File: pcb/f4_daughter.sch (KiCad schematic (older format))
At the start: 0 parts

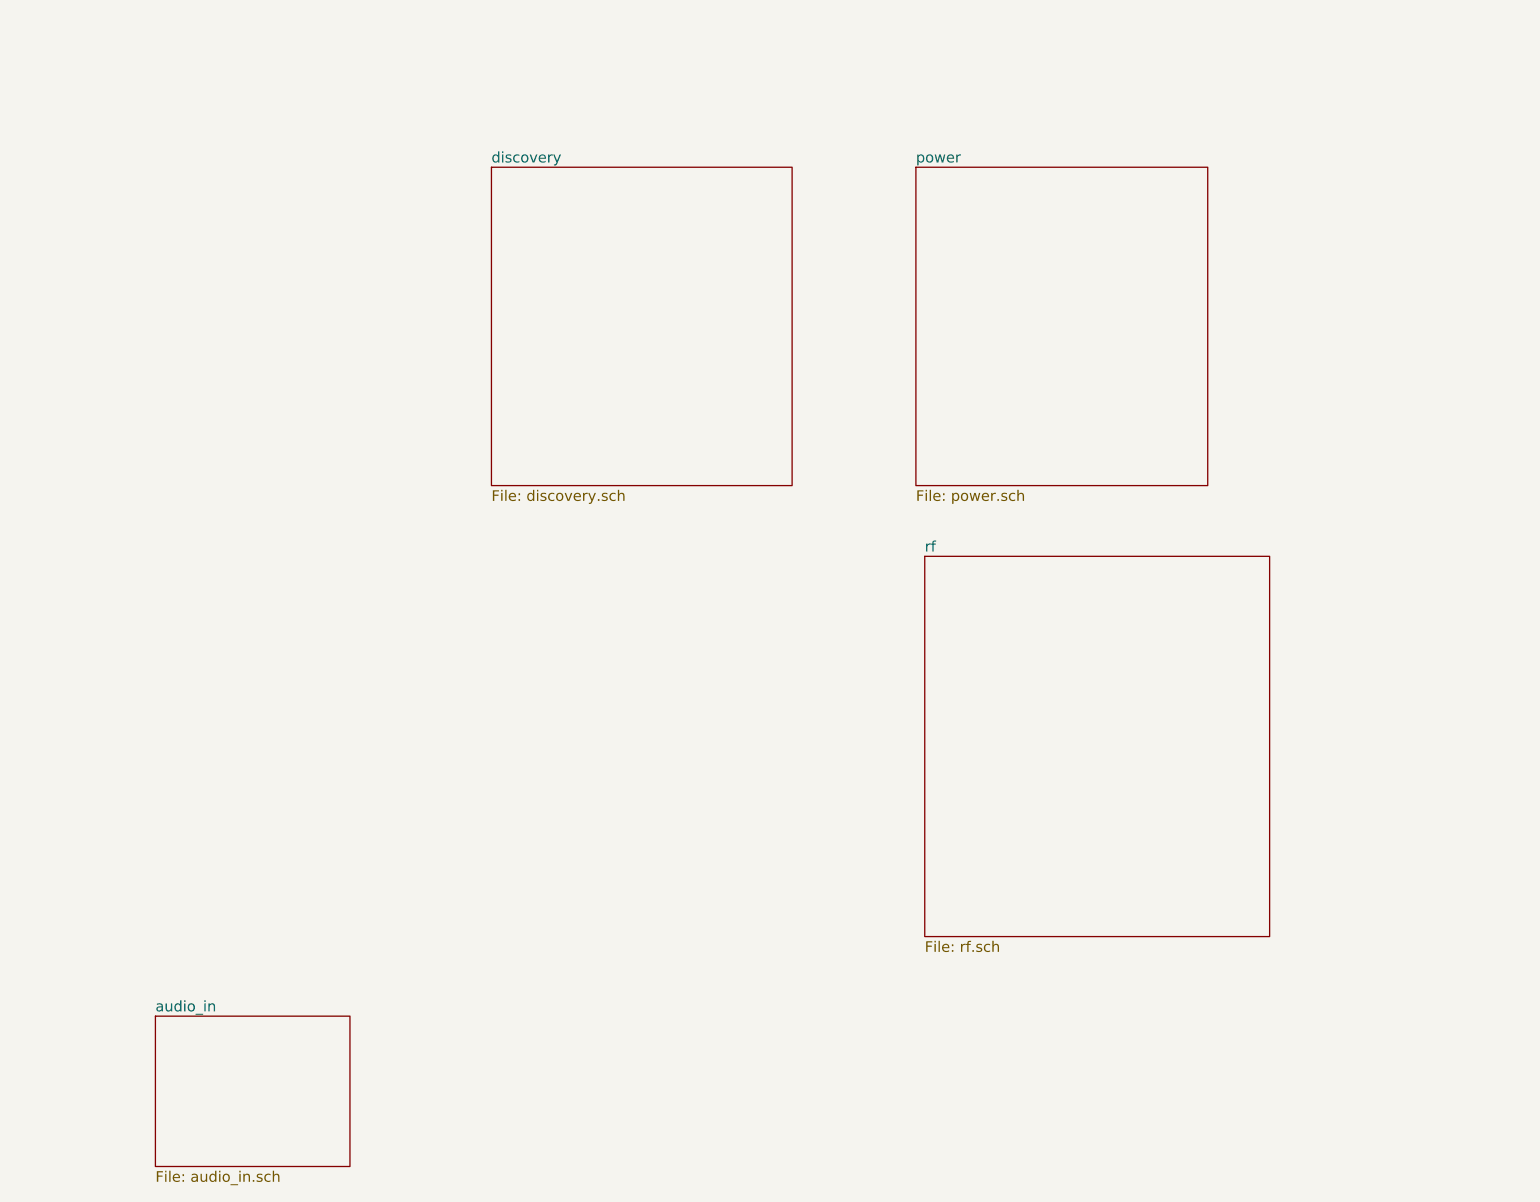
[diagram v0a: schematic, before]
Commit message: Broke up schematic in a more modular fashion -- Added LCD footprint
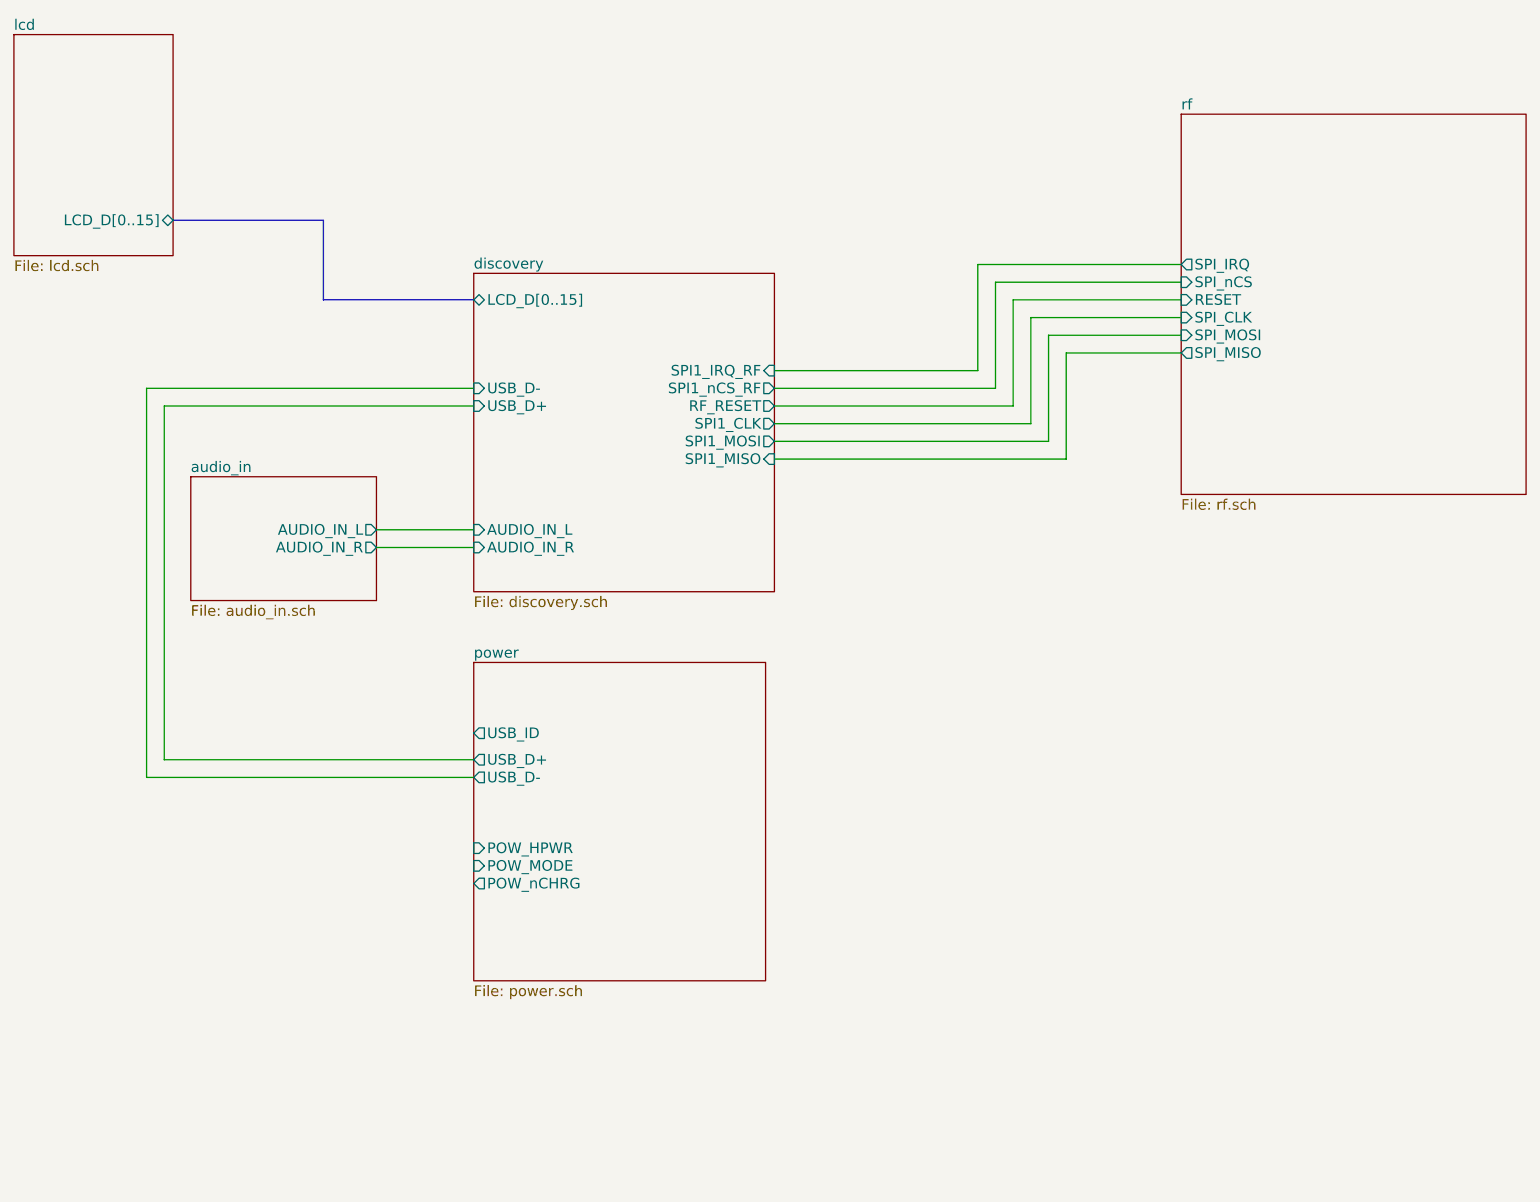
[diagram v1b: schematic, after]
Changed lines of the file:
@@
-EESchema Schematic File Version 2  date Thu 26 Jul 2012 11:54:13 PM EDT
+EESchema Schematic File Version 2  date Tue 31 Jul 2012 10:29:35 PM EDT
 LIBS:power
 LIBS:device
@@
 EELAYER 25  0
 EELAYER END
-$Descr A4 11693 8268
+$Descr A4 11700 8267
 encoding utf-8
-Sheet 1 5
+Sheet 1 6
 Title ""
-Date "27 jul 2012"
+Date "1 aug 2012"
 Rev ""
 Comp ""
@@
 Comment4 ""
 $EndDescr
+Wire Wire Line
+	3950 2700 2100 2700
+Wire Wire Line
+	2100 2700 2100 4900
+Wire Wire Line
+	2100 4900 3950 4900
+Wire Wire Line
+	3950 3600 3400 3600
+Wire Bus Line
+	2250 1750 3100 1750
+Wire Bus Line
+	3100 1750 3100 2200
+Wire Bus Line
+	3100 2200 3950 2200
+Wire Wire Line
+	7950 2400 7200 2400
+Wire Wire Line
+	7200 2400 7200 3000
+Wire Wire Line
+	7200 3000 5650 3000
+Wire Wire Line
+	7950 2200 7000 2200
+Wire Wire Line
+	7000 2200 7000 2800
+Wire Wire Line
+	7000 2800 5650 2800
+Wire Wire Line
+	7950 2000 6800 2000
+Wire Wire Line
+	6800 2000 6800 2600
+Wire Wire Line
+	6800 2600 5650 2600
+Wire Wire Line
+	5650 2700 6900 2700
+Wire Wire Line
+	6900 2700 6900 2100
+Wire Wire Line
+	6900 2100 7950 2100
+Wire Wire Line
+	5650 2900 7100 2900
+Wire Wire Line
+	7100 2900 7100 2300
+Wire Wire Line
+	7100 2300 7950 2300
+Wire Wire Line
+	5650 3100 7300 3100
+Wire Wire Line
+	7300 3100 7300 2500
+Wire Wire Line
+	7300 2500 7950 2500
+Wire Wire Line
+	3400 3500 3950 3500
+Wire Wire Line
+	3950 4800 2200 4800
+Wire Wire Line
+	2200 4800 2200 2800
+Wire Wire Line
+	2200 2800 3950 2800
 $Sheet
-S 6500 3650 1950 2150
+S 7950 1150 1950 2150
 U 500DC44C
 F0 "rf" 60
 F1 "rf.sch" 60
+F2 "RESET" I L 7950 2200 60
+F3 "SPI_IRQ" O L 7950 2000 60
+F4 "SPI_MOSI" I L 7950 2400 60
+F5 "SPI_MISO" O L 7950 2500 60
+F6 "SPI_CLK" I L 7950 2300 60
+F7 "SPI_nCS" I L 7950 2100 60
 $EndSheet
 $Sheet
-S 4050 1450 1700 1800
+S 3950 2050 1700 1800
 U 500B6AFA
 F0 "discovery" 60
 F1 "discovery.sch" 60
+F2 "USB_D-" I L 3950 2700 60
+F3 "USB_D+" I L 3950 2800 60
+F4 "AUDIO_IN_L" I L 3950 3500 60
+F5 "AUDIO_IN_R" I L 3950 3600 60
+F6 "LCD_D[0..15]" B L 3950 2200 60
+F7 "SPI1_IRQ_RF" I R 5650 2600 60
+F8 "SPI1_nCS_RF" O R 5650 2700 60
+F9 "RF_RESET" O R 5650 2800 60
+F10 "SPI1_CLK" O R 5650 2900 60
+F11 "SPI1_MOSI" O R 5650 3000 60
+F12 "SPI1_MISO" I R 5650 3100 60
 $EndSheet
 $Sheet
-S 6450 1450 1650 1800
+S 1350 700  900  1250
+U 50188B6E
+F0 "lcd" 60
+F1 "lcd.sch" 60
+F2 "LCD_D[0..15]" B R 2250 1750 60
+$EndSheet
+$Sheet
+S 3950 4250 1650 1800
 U 500B69F1
 F0 "power" 60
 F1 "power.sch" 60
+F2 "USB_ID" O L 3950 4650 60
+F3 "USB_D+" O L 3950 4800 60
+F4 "USB_D-" O L 3950 4900 60
+F5 "POW_MODE" I L 3950 5400 60
+F6 "POW_nCHRG" O L 3950 5500 60
+F7 "POW_HPWR" I L 3950 5300 60
 $EndSheet
 $Sheet
-S 2150 6250 1100 850
+S 2350 3200 1050 700
 U 5010D8BD
 F0 "audio_in" 60
 F1 "audio_in.sch" 60
+F2 "AUDIO_IN_L" O R 3400 3500 60
+F3 "AUDIO_IN_R" O R 3400 3600 60
 $EndSheet
 $EndSCHEMATC

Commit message: Connected the power pins to some free GPIOs
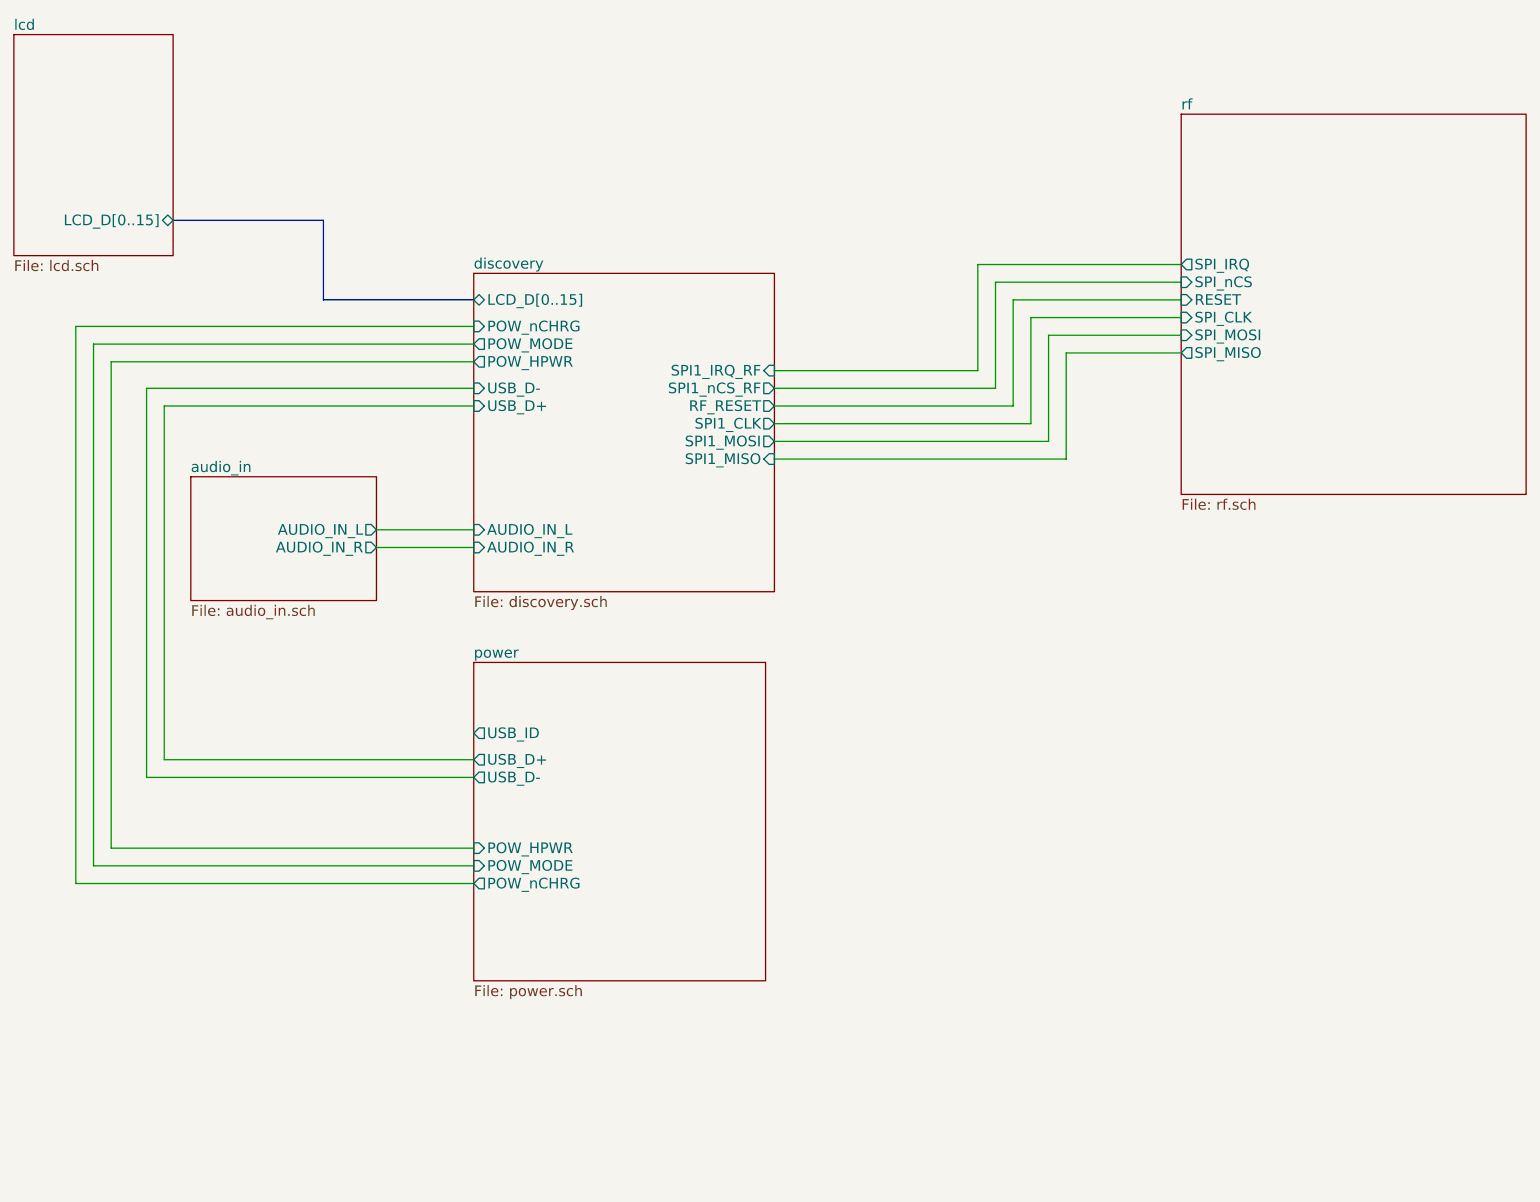
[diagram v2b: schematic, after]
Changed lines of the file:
@@
-EESchema Schematic File Version 2  date Tue 31 Jul 2012 10:29:35 PM EDT
+EESchema Schematic File Version 2  date 8/16/2012 11:22:19 AM
 LIBS:power
 LIBS:device
@@
 LIBS:valves
 LIBS:f4_daughter
-LIBS:f4_daughter-cache
 EELAYER 25  0
 EELAYER END
@@
 Sheet 1 6
 Title ""
-Date "1 aug 2012"
+Date "16 aug 2012"
 Rev ""
 Comp ""
@@
 $EndDescr
 Wire Wire Line
-	3950 2700 2100 2700
+	3950 5300 1900 5300
 Wire Wire Line
-	2100 2700 2100 4900
+	1900 5300 1900 2550
 Wire Wire Line
-	2100 4900 3950 4900
+	1900 2550 3950 2550
 Wire Wire Line
-	3950 3600 3400 3600
-Wire Bus Line
-	2250 1750 3100 1750
-Wire Bus Line
-	3100 1750 3100 2200
-Wire Bus Line
-	3100 2200 3950 2200
+	3950 5500 1700 5500
 Wire Wire Line
-	7950 2400 7200 2400
+	1700 5500 1700 2350
 Wire Wire Line
-	7200 2400 7200 3000
+	1700 2350 3950 2350
 Wire Wire Line
-	7200 3000 5650 3000
+	3950 2800 2200 2800
 Wire Wire Line
-	7950 2200 7000 2200
+	2200 2800 2200 4800
 Wire Wire Line
-	7000 2200 7000 2800
-Wire Wire Line
-	7000 2800 5650 2800
-Wire Wire Line
-	7950 2000 6800 2000
-Wire Wire Line
-	6800 2000 6800 2600
-Wire Wire Line
-	6800 2600 5650 2600
-Wire Wire Line
-	5650 2700 6900 2700
-Wire Wire Line
-	6900 2700 6900 2100
-Wire Wire Line
-	6900 2100 7950 2100
-Wire Wire Line
-	5650 2900 7100 2900
-Wire Wire Line
-	7100 2900 7100 2300
-Wire Wire Line
-	7100 2300 7950 2300
-Wire Wire Line
-	5650 3100 7300 3100
-Wire Wire Line
-	7300 3100 7300 2500
-Wire Wire Line
-	7300 2500 7950 2500
+	2200 4800 3950 4800
 Wire Wire Line
 	3400 3500 3950 3500
 Wire Wire Line
-	3950 4800 2200 4800
+	7950 2500 7300 2500
 Wire Wire Line
-	2200 4800 2200 2800
+	7300 2500 7300 3100
 Wire Wire Line
-	2200 2800 3950 2800
+	7300 3100 5650 3100
+Wire Wire Line
+	7950 2300 7100 2300
+Wire Wire Line
+	7100 2300 7100 2900
+Wire Wire Line
+	7100 2900 5650 2900
+Wire Wire Line
+	7950 2100 6900 2100
+Wire Wire Line
+	6900 2100 6900 2700
+Wire Wire Line
+	6900 2700 5650 2700
+Wire Wire Line
+	5650 2600 6800 2600
+Wire Wire Line
+	6800 2600 6800 2000
+Wire Wire Line
+	6800 2000 7950 2000
+Wire Wire Line
+	5650 2800 7000 2800
+Wire Wire Line
+	7000 2800 7000 2200
+Wire Wire Line
+	7000 2200 7950 2200
+Wire Wire Line
+	5650 3000 7200 3000
+Wire Wire Line
+	7200 3000 7200 2400
+Wire Wire Line
+	7200 2400 7950 2400
+Wire Bus Line
+	3950 2200 3100 2200
+Wire Bus Line
+	3100 2200 3100 1750
+Wire Bus Line
+	3100 1750 2250 1750
+Wire Wire Line
+	3950 3600 3400 3600
+Wire Wire Line
+	3950 4900 2100 4900
+Wire Wire Line
+	2100 4900 2100 2700
+Wire Wire Line
+	2100 2700 3950 2700
+Wire Wire Line
+	3950 2450 1800 2450
+Wire Wire Line
+	1800 2450 1800 5400
+Wire Wire Line
+	1800 5400 3950 5400
 $Sheet
 S 7950 1150 1950 2150
@@
 F11 "SPI1_MOSI" O R 5650 3000 60
 F12 "SPI1_MISO" I R 5650 3100 60
+F13 "POW_HPWR" O L 3950 2550 60
+F14 "POW_MODE" O L 3950 2450 60
+F15 "POW_nCHRG" I L 3950 2350 60
 $EndSheet
 $Sheet
